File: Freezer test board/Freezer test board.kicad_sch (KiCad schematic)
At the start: 20 parts, among them J1 Conn_02x02_Odd_Even, J2 Conn_02x20_Odd_Even, J3 284391-3, J4 284391-3, J5 284391-3, J6 284391-3, J7 284391-3, J8 284391-3, J9 284391-3

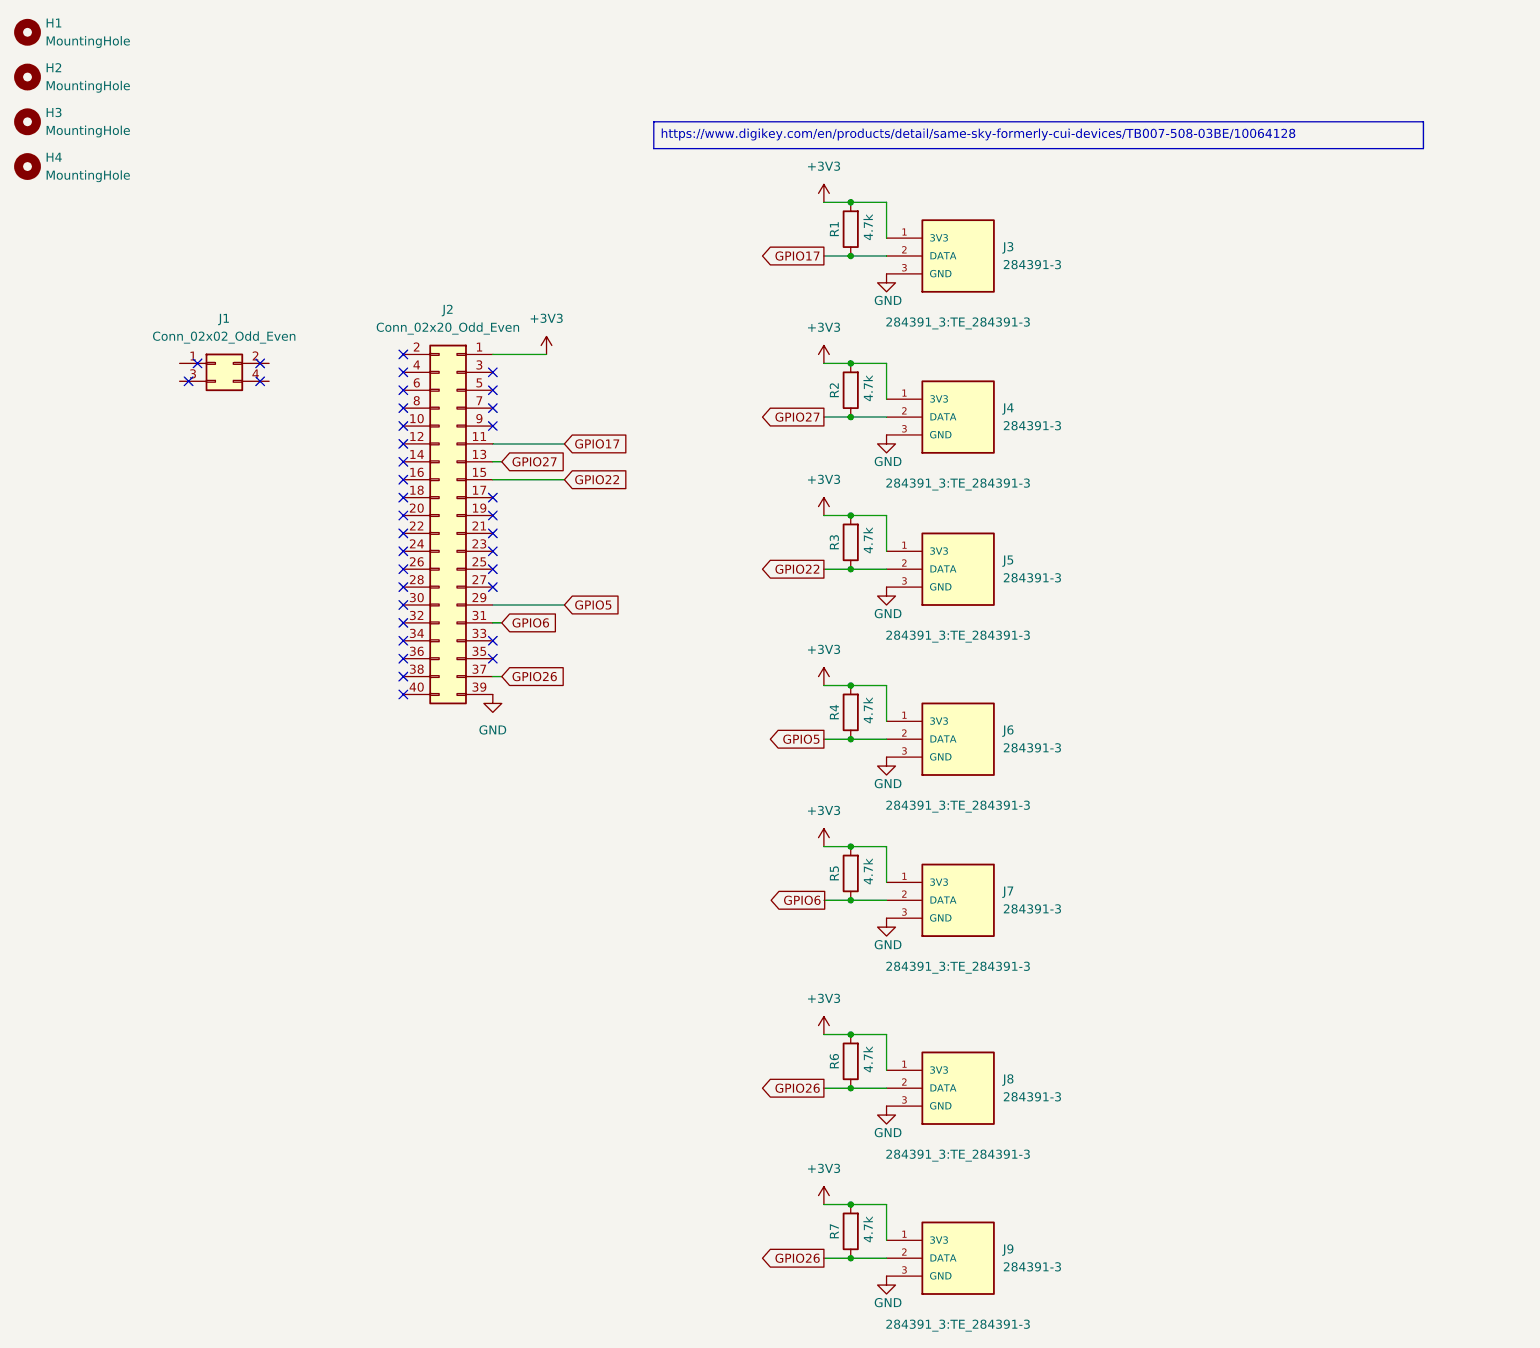
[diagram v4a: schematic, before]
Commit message: Changed to 1 GPIO and cleaned up the connections
All of the Signals connections have been changed to go to One GPIO pin per the request of the software person. connections were cleaned up because they were all over the place.
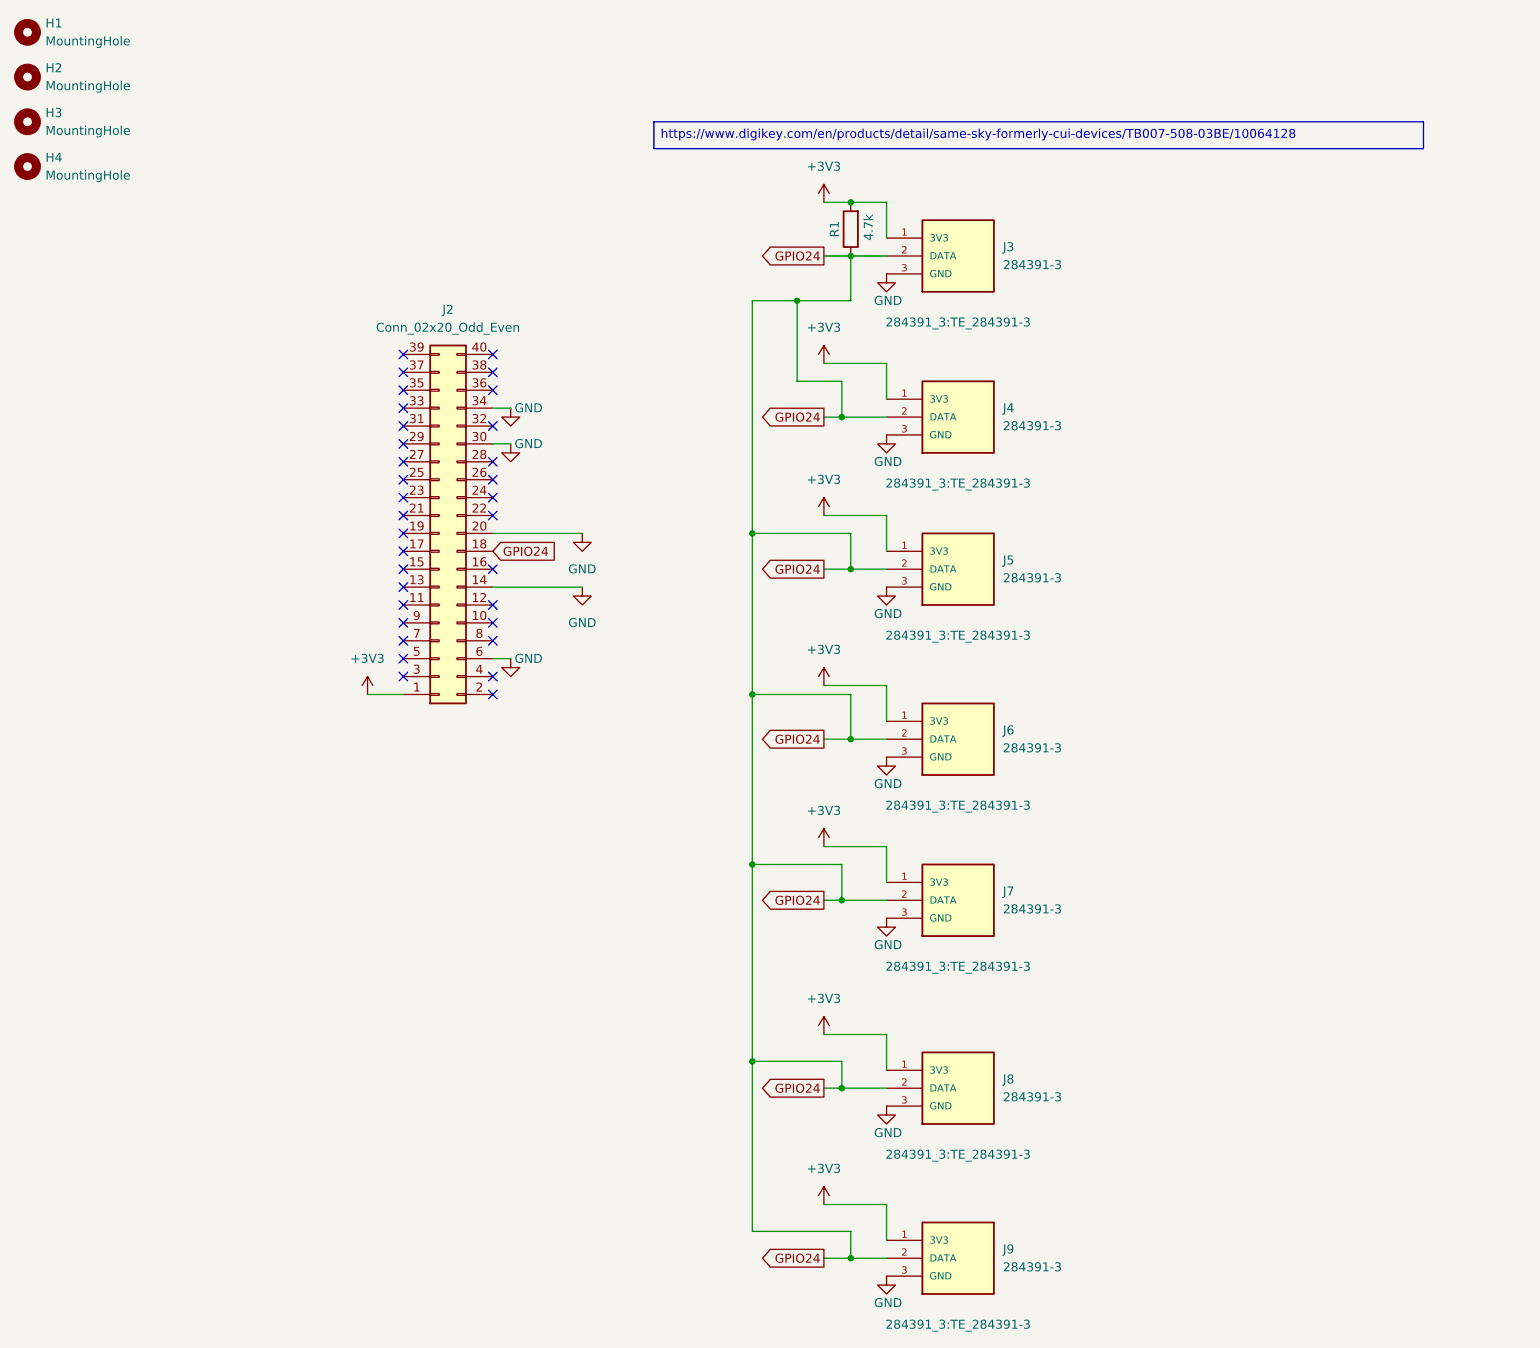
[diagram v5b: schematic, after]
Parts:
- removed J1: Conn_02x02_Odd_Even, Connector_PinSocket_2.54mm:PinSocket_2x02_P2.54mm_Vertical, symbol Connector_Generic:Conn_02x02_Odd_Even
- removed R2, R3, R4, R5, R6, R7: 4.7k, Resistor_SMD:R_0201_0603Metric, symbol Device:R
- R1: footprint Resistor_SMD:R_0201_0603Metric -> Resistor_THT:R_Axial_DIN0204_L3.6mm_D1.6mm_P5.08mm_Horizontal
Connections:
- net GND: now also J2.14 (Pin_14), J2.20 (Pin_20), J2.30 (Pin_30), J2.34 (Pin_34), J2.6 (Pin_6); no longer J2.39 (Pin_39)
- net GPIO24: now reaches J2.18 (Pin_18)
- net GPIO24: now also J3.2 (DATA), J4.2 (DATA), J5.2 (DATA), J6.2 (DATA), J7.2 (DATA), J8.2 (DATA), J9.2 (DATA), R1.1
- removed net GPIO17: J2.11 (Pin_11), J3.2 (DATA), R1.1
- net GPIO22: no longer names the net of J2.15 (Pin_15)
- net GPIO22: no longer J5.2 (DATA)
- removed net GPIO26: J2.37 (Pin_37), J8.2 (DATA), J9.2 (DATA)
- net GPIO27: no longer names the net of J2.13 (Pin_13)
- net GPIO27: no longer J4.2 (DATA)
- net GPIO5: no longer names the net of J2.29 (Pin_29)
- net GPIO5: no longer J6.2 (DATA)
- net GPIO6: no longer names the net of J2.31 (Pin_31)
- net GPIO6: no longer J7.2 (DATA)
- no-connect marks 36 -> 33

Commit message: Finished Product
Its done, all connections are routed and essential memes have been added.
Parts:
- added R2, R3, R4, R5, R6, R7: 4.7k, Resistor_THT:R_Axial_DIN0204_L3.6mm_D1.6mm_P5.08mm_Horizontal, symbol Device:R
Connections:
- net +3V3: now also R2.2, R3.2, R4.2, R5.2, R6.2, R7.2
- net GPIO24: now also R3.1; no longer J3.2 (DATA), J4.2 (DATA), J6.2 (DATA), J7.2 (DATA), J8.2 (DATA), J9.2 (DATA), R1.1
- net GPIO17: now reaches J2.11 (Pin_11)
- net GPIO17: now also J7.2 (DATA), R5.1
- net GPIO23: now reaches J2.16 (Pin_16)
- net GPIO23: now also J6.2 (DATA), R4.1
- net GPIO25: now reaches J2.22 (Pin_22)
- net GPIO25: now also J4.2 (DATA), R2.1
- net GPIO5: now reaches J2.29 (Pin_29)
- net GPIO5: now also J8.2 (DATA), R6.1
- net GPIO6: now reaches J2.31 (Pin_31)
- net GPIO6: now also J9.2 (DATA), R7.1
- net GPIO16: now reaches J2.36 (Pin_36)
- net GPIO16: now also J3.2 (DATA), R1.1
- no-connect marks 33 -> 27

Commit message: Revert "Finished Product"
This reverts commit 4c5b83d13ff1ed3163e33f6f8de5480cfa8905a7.
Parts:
- removed R2, R3, R4, R5, R6, R7: 4.7k, Resistor_THT:R_Axial_DIN0204_L3.6mm_D1.6mm_P5.08mm_Horizontal, symbol Device:R
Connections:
- net GPIO24: now also J3.2 (DATA), J4.2 (DATA), J6.2 (DATA), J7.2 (DATA), J8.2 (DATA), J9.2 (DATA), R1.1
- removed net GPIO16: J2.36 (Pin_36), J3.2 (DATA), R1.1
- net GPIO17: no longer names the net of J2.11 (Pin_11)
- net GPIO17: no longer J7.2 (DATA)
- net GPIO23: no longer names the net of J2.16 (Pin_16)
- net GPIO23: no longer J6.2 (DATA)
- net GPIO25: no longer names the net of J2.22 (Pin_22)
- net GPIO25: no longer J4.2 (DATA)
- net GPIO5: no longer names the net of J2.29 (Pin_29)
- net GPIO5: no longer J8.2 (DATA)
- net GPIO6: no longer names the net of J2.31 (Pin_31)
- net GPIO6: no longer J9.2 (DATA)
- no-connect marks 27 -> 33

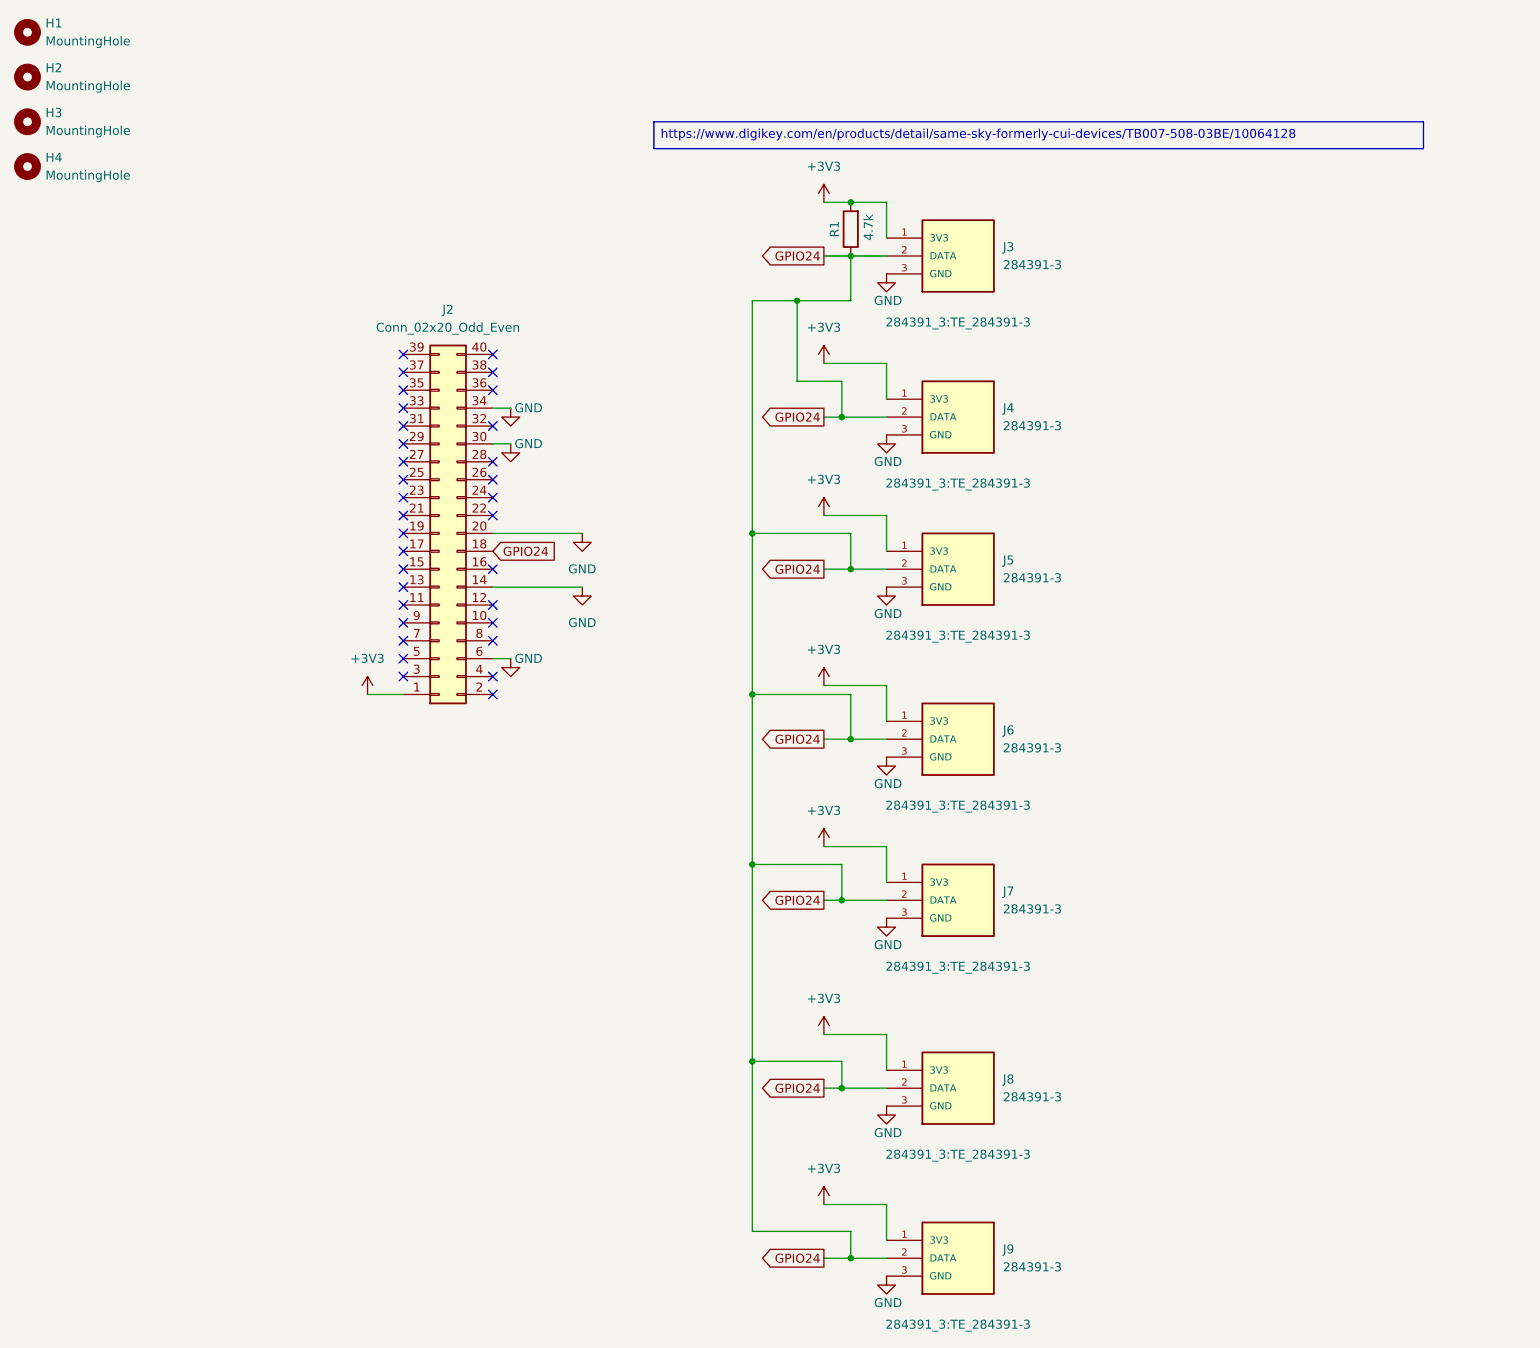
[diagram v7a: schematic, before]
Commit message: fixed?
reverted to the Tri's previous push and then re did the signal tracks, re organized the resistors and terminal blocks. Other than everything is the exact same
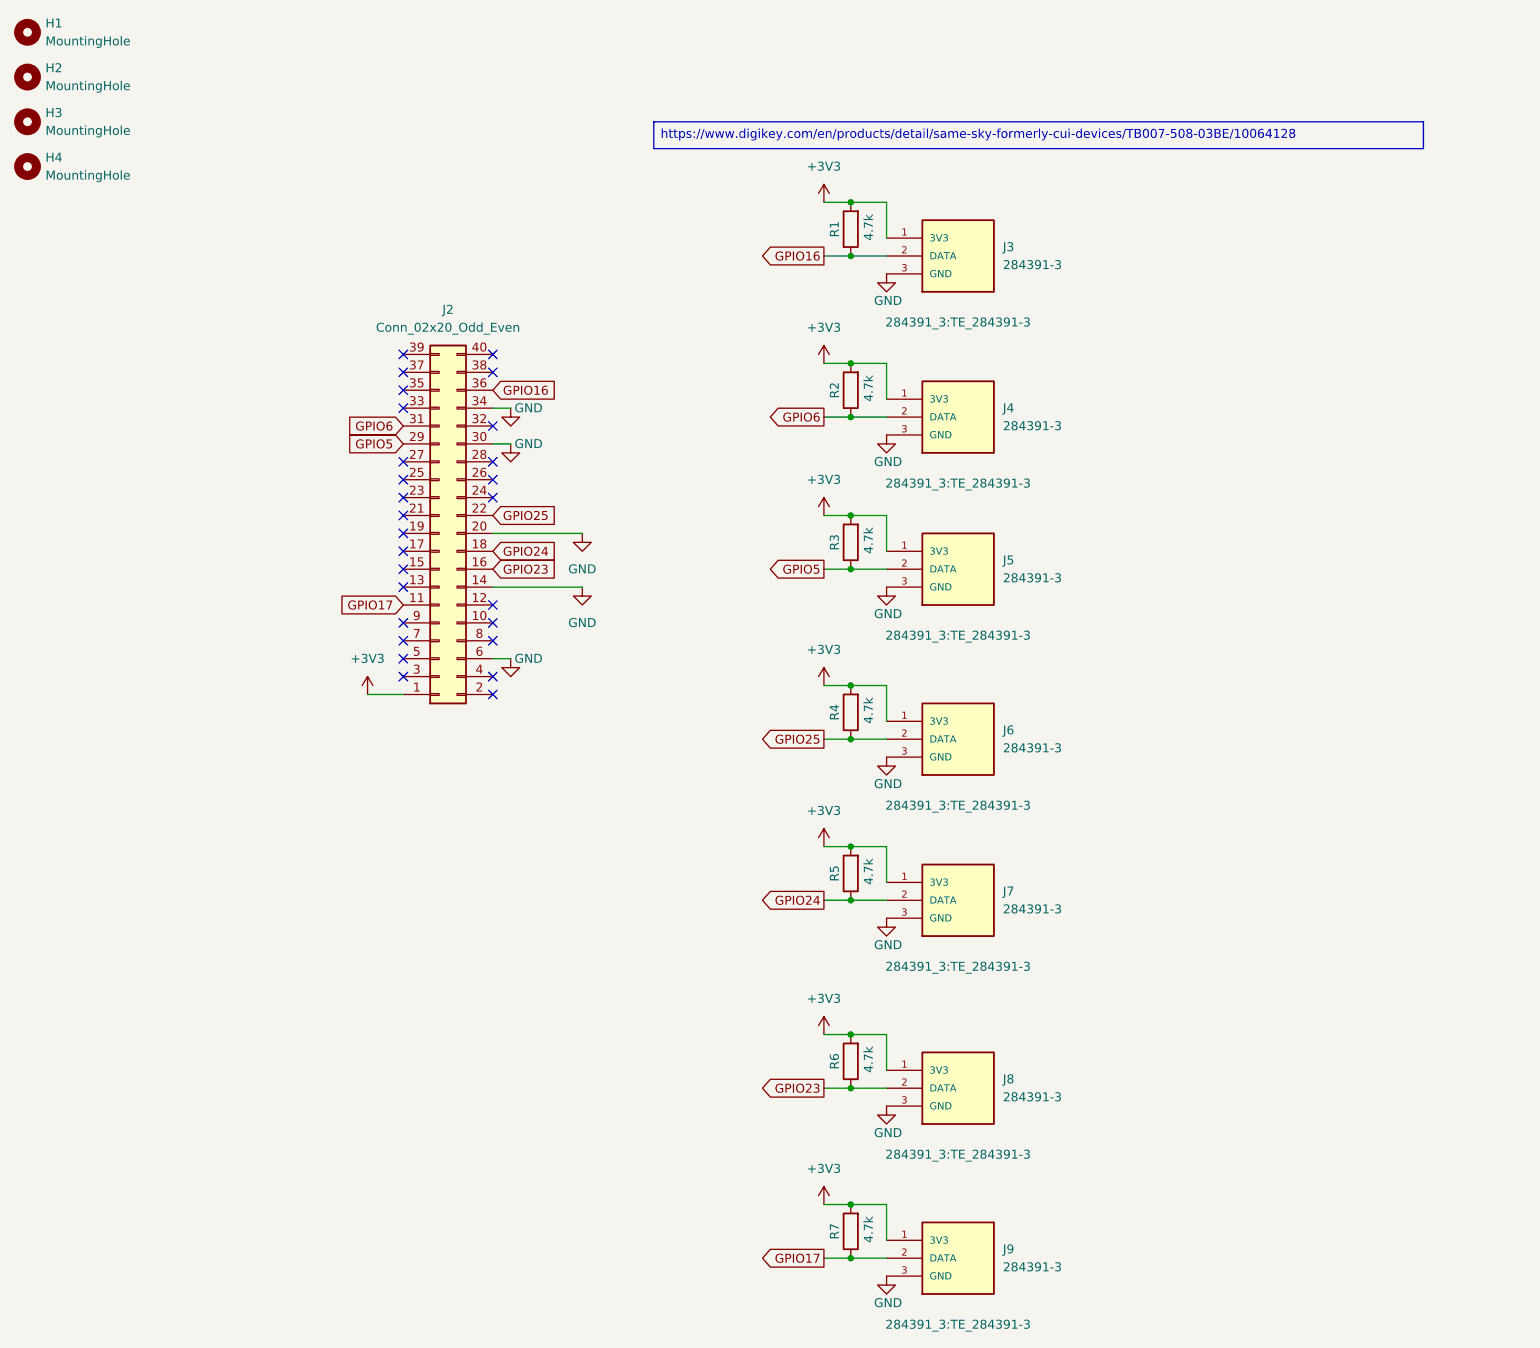
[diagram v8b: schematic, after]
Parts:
- added R2, R3, R4, R5, R6, R7: 4.7k, Resistor_THT:R_Axial_DIN0204_L3.6mm_D1.6mm_P5.08mm_Horizontal, symbol Device:R
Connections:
- net +3V3: now also R2.2, R3.2, R4.2, R5.2, R6.2, R7.2
- net GPIO24: now also R5.1; no longer J3.2 (DATA), J4.2 (DATA), J5.2 (DATA), J6.2 (DATA), J8.2 (DATA), J9.2 (DATA), R1.1
- net GPIO17: now reaches J2.11 (Pin_11)
- net GPIO17: now also J9.2 (DATA), R7.1
- net GPIO23: now reaches J2.16 (Pin_16)
- net GPIO23: now also J8.2 (DATA), R6.1
- net GPIO25: now reaches J2.22 (Pin_22)
- net GPIO25: now also J6.2 (DATA), R4.1
- net GPIO5: now reaches J2.29 (Pin_29)
- net GPIO5: now also J5.2 (DATA), R3.1
- net GPIO6: now reaches J2.31 (Pin_31)
- net GPIO6: now also J4.2 (DATA), R2.1
- net GPIO16: now reaches J2.36 (Pin_36)
- net GPIO16: now also J3.2 (DATA), R1.1
- no-connect marks 33 -> 27
